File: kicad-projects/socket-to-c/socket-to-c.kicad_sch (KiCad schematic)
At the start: 4 parts, among them J1 Racklet_USBSocket_02x06, J2 USB_C_Receptacle_USB2.0

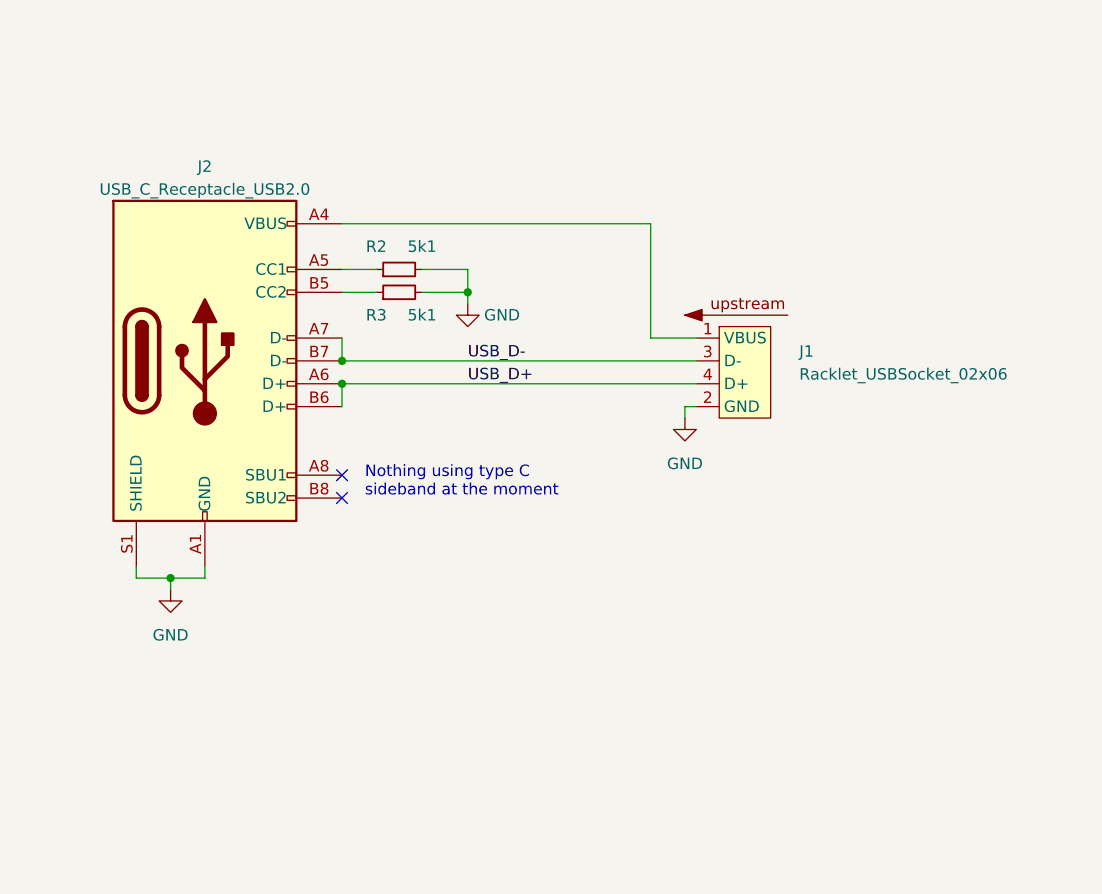
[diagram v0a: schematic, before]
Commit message: socket-to-c: add banana plugs
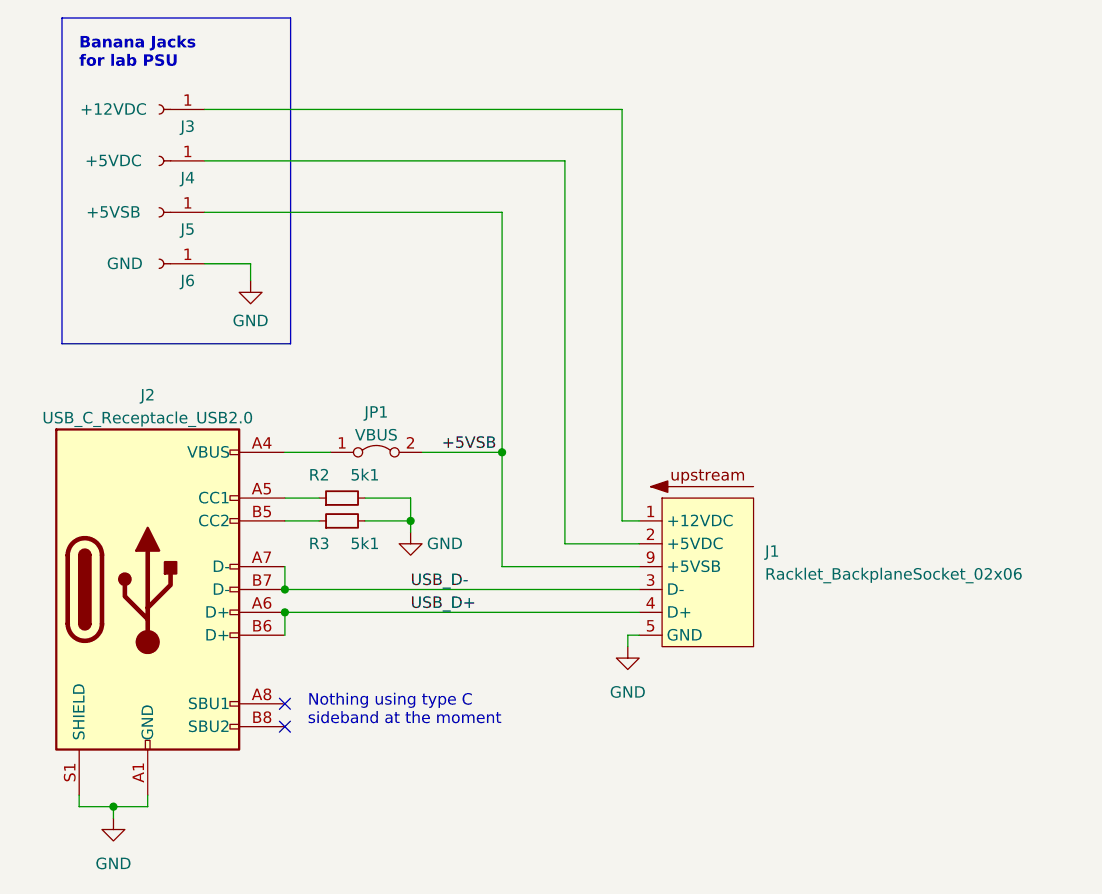
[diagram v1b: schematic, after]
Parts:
- removed J1: Racklet_USBSocket_02x06, racklet:Racklet_USBSocket_02x06, symbol racklet:Racklet_USBSocket_02x06
- added J1: Racklet_BackplaneSocket_02x06, racklet:Racklet_BackplaneSocket_02x06, symbol racklet:Racklet_BackplaneSocket_02x06
- added J3: +12VDC, Connector:Banana_Cliff_FCR7350x_S16N-PC_Horizontal, symbol Connector:Conn_01x01_Socket
- added J4: +5VDC, Connector:Banana_Cliff_FCR7350x_S16N-PC_Horizontal, symbol Connector:Conn_01x01_Socket
- added J5: +5VSB, Connector:Banana_Cliff_FCR7350x_S16N-PC_Horizontal, symbol Connector:Conn_01x01_Socket
- added J6: GND, Connector:Banana_Cliff_FCR7350x_S16N-PC_Horizontal, symbol Connector:Conn_01x01_Socket
- added JP1: VBUS, Connector_PinHeader_2.54mm:PinHeader_1x02_P2.54mm_Vertical, symbol Jumper:Jumper_2_Bridged
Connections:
- net GND: now also J1.10 (GND), J1.11 (GND), J1.12 (GND), J1.5 (GND), J1.6 (GND), J6.1 (Pin_1)
- net USB_D+: now also J1.4 (D+)
- net USB_D-: now also J1.3 (D-)
- net VBUS: no longer names the net of J2.A4 (VBUS), J2.A9 (VBUS), J2.B4 (VBUS), J2.B9 (VBUS)
- net VBUS: now also JP1.1 (A)
- new net +12VDC: J1.1 (+12VDC), J1.7 (+12VDC), J3.1 (Pin_1)
- new net +5VDC: J1.2 (+5VDC), J1.8 (+5VDC), J4.1 (Pin_1)
- new net +5VSB: J1.9 (+5VSB), J5.1 (Pin_1), JP1.2 (B)
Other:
- note added: "Banana Jacks for lab PSU"
- moved on the sheet: J2, R2, R3
